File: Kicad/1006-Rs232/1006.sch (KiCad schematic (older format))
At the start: 8 parts, among them J1 DB9, P1 CONN_4, U1 TRS322ECN

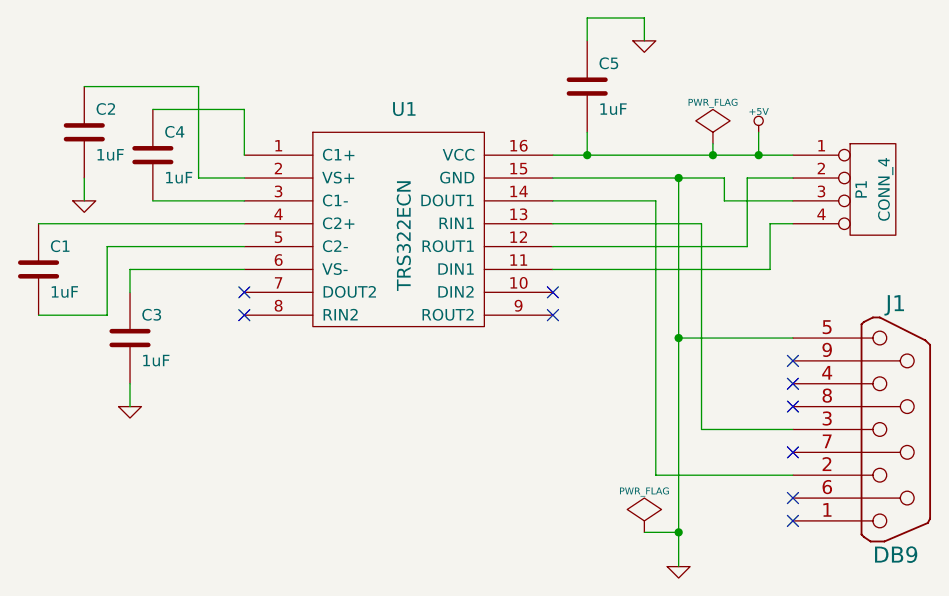
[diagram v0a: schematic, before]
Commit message: Added solenoid wiring diagram to interface document.  (Now in Docs directory)  Fixed RS232 interface pinout match solenoid and input cards.  Added build.bat to create zip files for each project.  Added build_notes.txt for each project.  Stored zipped gerber files into the repository.  Created power supply board, and Raspberry Pi shield.  Added 74LVC245 to parts library.
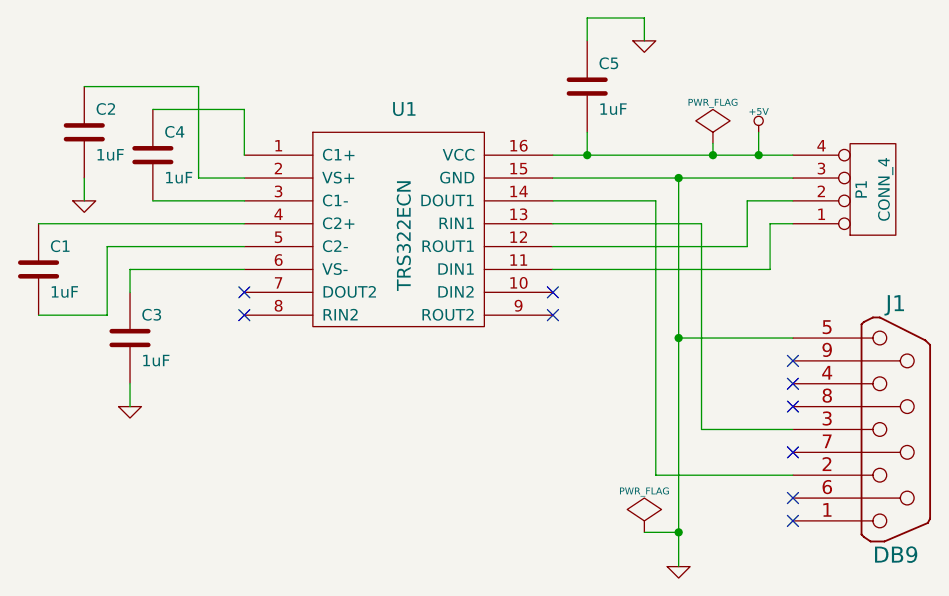
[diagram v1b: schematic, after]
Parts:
- C1, C2, C3, C4, C5: Field4 (none) -> CAP1.00uTH
- P1: Field4 (none) -> CON1x4x2.54mmVTTHL
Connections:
- net +5V: now also P1.4 (P4); no longer P1.1 (P1)
- net at U1.11 (DIN1): now also P1.1 (P1); no longer P1.4 (P4)
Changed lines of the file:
@@
-EESchema Schematic File Version 2  date 1/18/2013 3:12:57 PM
+EESchema Schematic File Version 2
 LIBS:commonpart
 LIBS:power
@@
 LIBS:valves
 LIBS:1006-cache
-EELAYER 25  0
+EELAYER 27 0
 EELAYER END
 $Descr A 11000 8500
@@
 Sheet 1 1
 Title "RS232 Interface"
-Date "27 apr 2012"
-Rev "-"
+Date "4 jan 2014"
+Rev "A"
 Comp "Open Pinball Project"
 Comment1 ""
@@
 	4650 3750 4800 3750
 Wire Wire Line
-	5300 2200 5100 2200
-Wire Wire Line
-	5100 2200 5100 2500
-Wire Wire Line
 	5100 2500 4250 2500
 Connection ~ 4800 2900
@@
 Wire Wire Line
 	4800 2200 4800 3900
-Wire Wire Line
-	4250 2200 5000 2200
-Wire Wire Line
-	5000 2200 5000 2300
-Wire Wire Line
-	5000 2300 5300 2300
 Connection ~ 4800 2200
 Wire Wire Line
@@
 F 0 "#PWR01" H 4650 1600 30  0001 C CNN
 F 1 "GND" H 4650 1530 30  0001 C CNN
+F 2 "" H 4650 1600 60  0001 C CNN
+F 3 "" H 4650 1600 60  0001 C CNN
 	1    4650 1600
 	1    0    0    -1
@@
 F 0 "C5" H 4450 1900 50  0000 L CNN
 F 1 "1uF" H 4450 1700 50  0000 L CNN
+F 2 "" H 4400 1800 60  0001 C CNN
+F 3 "" H 4400 1800 60  0001 C CNN
+F 4 "CAP1.00uTH" H 4400 1800 60  0001 C CNN "Field4"
 	1    4400 1800
 	1    0    0    -1
@@
 F 0 "#FLG02" H 4650 3845 30  0001 C CNN
 F 1 "PWR_FLAG" H 4650 3930 30  0000 C CNN
+F 2 "" H 4650 3750 60  0001 C CNN
+F 3 "" H 4650 3750 60  0001 C CNN
 	1    4650 3750
 	1    0    0    -1
@@
 F 0 "#FLG03" H 4950 2145 30  0001 C CNN
 F 1 "PWR_FLAG" H 4950 2230 30  0000 C CNN
+F 2 "" H 4950 2050 60  0001 C CNN
+F 3 "" H 4950 2050 60  0001 C CNN
 	1    4950 2050
 	1    0    0    -1
@@
 F 0 "J1" H 5750 3850 70  0000 C CNN
 F 1 "DB9" H 5750 2750 70  0000 C CNN
+F 2 "" H 5750 3300 60  0001 C CNN
+F 3 "" H 5750 3300 60  0001 C CNN
 	1    5750 3300
 	1    0    0    -1
@@
 F 0 "P1" V 5600 2250 50  0000 C CNN
 F 1 "CONN_4" V 5700 2250 50  0000 C CNN
+F 2 "" H 5650 2250 60  0001 C CNN
+F 3 "" H 5650 2250 60  0001 C CNN
+F 4 "CON1x4x2.54mmVTTHL" V 5650 2250 60  0001 C CNN "Field4"
 	1    5650 2250
-	1    0    0    -1
+	1    0    0    1
 $EndComp
 $Comp
@@
 F 0 "#PWR04" H 4800 3900 30  0001 C CNN
 F 1 "GND" H 4800 3830 30  0001 C CNN
+F 2 "" H 4800 3900 60  0001 C CNN
+F 3 "" H 4800 3900 60  0001 C CNN
 	1    4800 3900
 	1    0    0    -1
@@
 F 0 "#PWR05" H 5150 2090 20  0001 C CNN
 F 1 "+5V" H 5150 2090 30  0000 C CNN
+F 2 "" H 5150 2000 60  0001 C CNN
+F 3 "" H 5150 2000 60  0001 C CNN
 	1    5150 2000
 	1    0    0    -1
@@
 F 0 "#PWR06" H 2400 3200 30  0001 C CNN
 F 1 "GND" H 2400 3130 30  0001 C CNN
+F 2 "" H 2400 3200 60  0001 C CNN
+F 3 "" H 2400 3200 60  0001 C CNN
 	1    2400 3200
 	1    0    0    -1
@@
 F 0 "C3" H 2450 3000 50  0000 L CNN
 F 1 "1uF" H 2450 2800 50  0000 L CNN
+F 2 "" H 2400 2900 60  0001 C CNN
+F 3 "" H 2400 2900 60  0001 C CNN
+F 4 "CAP1.00uTH" H 2400 2900 60  0001 C CNN "Field4"
 	1    2400 2900
 	1    0    0    -1
@@
 F 0 "C1" H 2050 2700 50  0000 L CNN
 F 1 "1uF" H 2050 2500 50  0000 L CNN
+F 2 "" H 2000 2600 60  0001 C CNN
+F 3 "" H 2000 2600 60  0001 C CNN
+F 4 "CAP1.00uTH" H 2000 2600 60  0001 C CNN "Field4"
 	1    2000 2600
 	1    0    0    -1
@@
 F 0 "#PWR07" H 2200 2300 30  0001 C CNN
 F 1 "GND" H 2200 2230 30  0001 C CNN
+F 2 "" H 2200 2300 60  0001 C CNN
+F 3 "" H 2200 2300 60  0001 C CNN
 	1    2200 2300
 	1    0    0    -1
@@
 F 0 "C2" H 2250 2100 50  0000 L CNN
 F 1 "1uF" H 2250 1900 50  0000 L CNN
+F 2 "" H 2200 2000 60  0001 C CNN
+F 3 "" H 2200 2000 60  0001 C CNN
+F 4 "CAP1.00uTH" H 2200 2000 60  0001 C CNN "Field4"
 	1    2200 2000
 	1    0    0    -1
@@
 F 0 "C4" H 2550 2200 50  0000 L CNN
 F 1 "1uF" H 2550 2000 50  0000 L CNN
+F 2 "" H 2500 2100 60  0001 C CNN
+F 3 "" H 2500 2100 60  0001 C CNN
+F 4 "CAP1.00uTH" H 2500 2100 60  0001 C CNN "Field4"
 	1    2500 2100
 	1    0    0    -1
@@
 F 0 "U1" H 3600 3000 60  0000 C CNN
 F 1 "TRS322ECN" V 3600 2450 60  0000 C CNN
+F 2 "" H 3600 2450 60  0001 C CNN
+F 3 "" H 3600 2450 60  0001 C CNN
 	1    3600 2450
 	1    0    0    -1
 $EndComp
+Wire Wire Line
+	4250 2200 5300 2200
+Wire Wire Line
+	5100 2500 5100 2300
+Wire Wire Line
+	5100 2300 5300 2300
 $EndSCHEMATC
